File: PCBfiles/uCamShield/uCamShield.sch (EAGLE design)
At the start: 9 parts

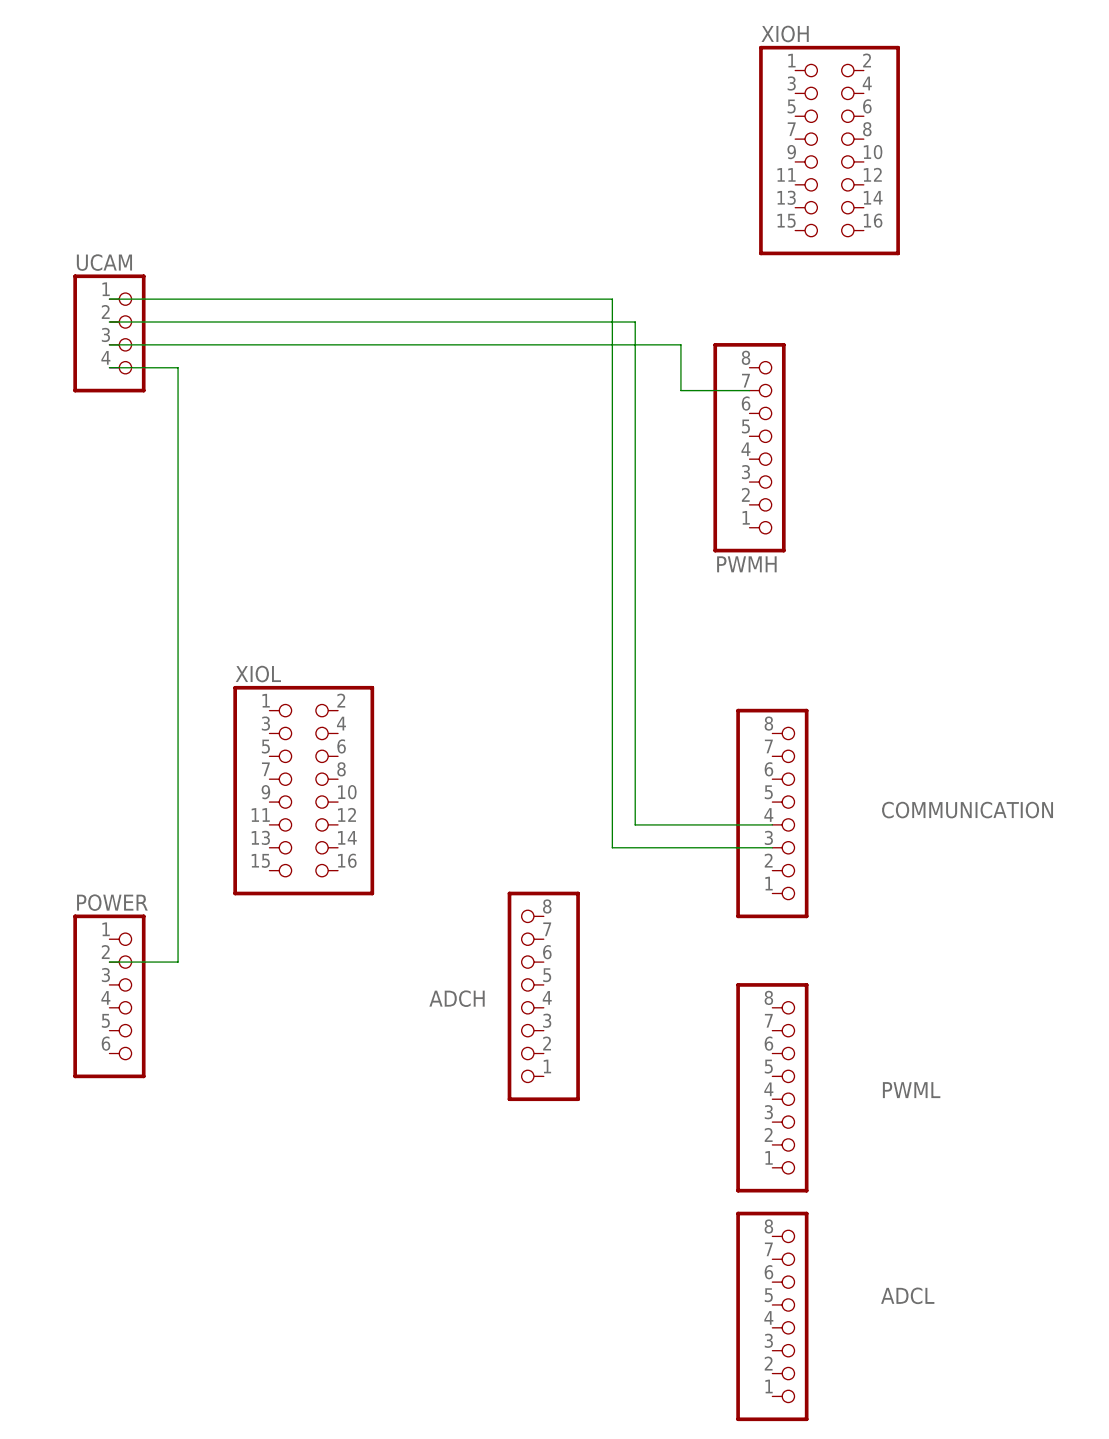
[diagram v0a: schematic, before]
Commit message: Fixed PCB file for uCam shield
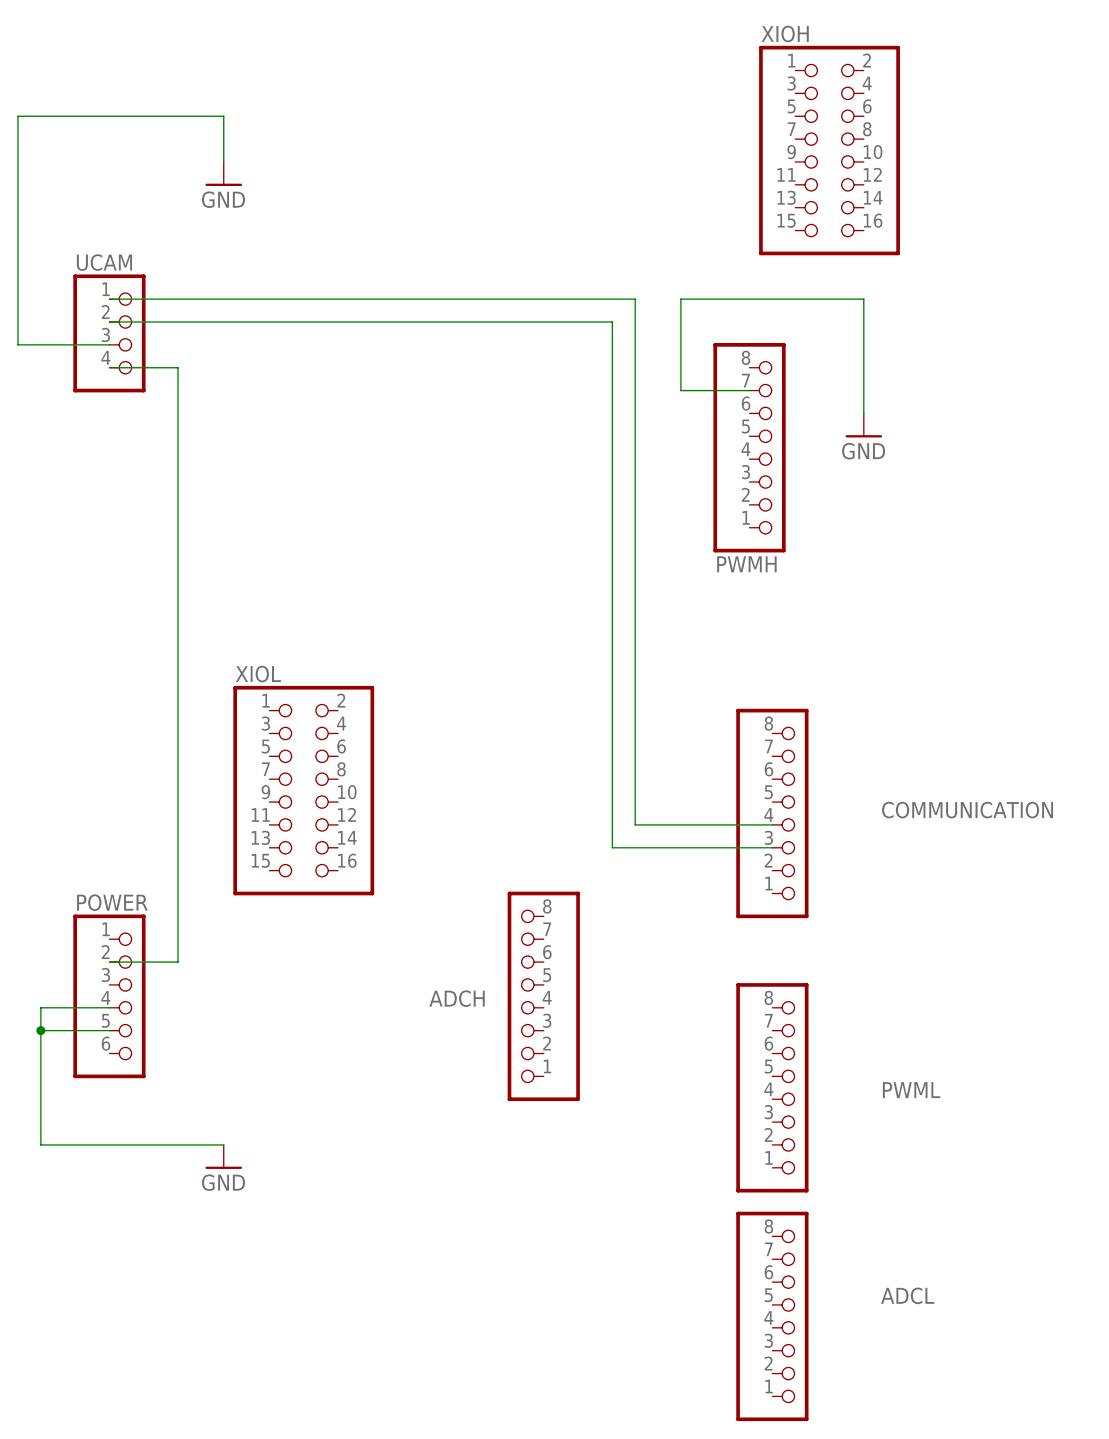
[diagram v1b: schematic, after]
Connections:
- removed net N$4: COMMUNICATION.3, UCAM.1
- new net GND: POWER.4, POWER.5, PWMH.7, UCAM.3
- net N$2: now also COMMUNICATION.4, UCAM.1; no longer PWMH.7, UCAM.3
- net N$3: now also COMMUNICATION.3; no longer COMMUNICATION.4
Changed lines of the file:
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@@
 <grid distance="0.1" unitdist="inch" unit="inch" style="lines" multiple="1" display="no" altdistance="0.01" altunitdist="inch" altunit="inch"/>
 <layers>
-<layer number="1" name="Top" color="4" fill="1" visible="yes" active="no"/>
-<layer number="2" name="Route2" color="1" fill="3" visible="yes" active="no"/>
-<layer number="3" name="Route3" color="4" fill="3" visible="yes" active="no"/>
-<layer number="14" name="Route14" color="1" fill="6" visible="yes" active="no"/>
-<layer number="15" name="Route15" color="4" fill="6" visible="yes" active="no"/>
-<layer number="16" name="Bottom" color="1" fill="1" visible="yes" active="no"/>
-<layer number="17" name="Pads" color="2" fill="1" visible="yes" active="no"/>
-<layer number="18" name="Vias" color="14" fill="1" visible="yes" active="no"/>
-<layer number="19" name="Unrouted" color="6" fill="1" visible="yes" active="no"/>
-<layer number="20" name="Dimension" color="15" fill="1" visible="yes" active="no"/>
-<layer number="21" name="tPlace" color="7" fill="1" visible="yes" active="no"/>
-<layer number="22" name="bPlace" color="7" fill="1" visible="yes" active="no"/>
-<layer number="23" name="tOrigins" color="15" fill="1" visible="yes" active="no"/>
-<layer number="24" name="bOrigins" color="15" fill="1" visible="yes" active="no"/>
-<layer number="25" name="tNames" color="7" fill="1" visible="yes" active="no"/>
-<layer number="26" name="bNames" color="7" fill="1" visible="yes" active="no"/>
-<layer number="27" name="tValues" color="7" fill="1" visible="yes" active="no"/>
-<layer number="28" name="bValues" color="7" fill="1" visible="yes" active="no"/>
+<layer number="1" name="Top" color="4" fill="1" visible="no" active="no"/>
+<layer number="2" name="Route2" color="1" fill="3" visible="no" active="no"/>
+<layer number="3" name="Route3" color="4" fill="3" visible="no" active="no"/>
+<layer number="14" name="Route14" color="1" fill="6" visible="no" active="no"/>
+<layer number="15" name="Route15" color="4" fill="6" visible="no" active="no"/>
+<layer number="16" name="Bottom" color="1" fill="1" visible="no" active="no"/>
+<layer number="17" name="Pads" color="2" fill="1" visible="no" active="no"/>
+<layer number="18" name="Vias" color="14" fill="1" visible="no" active="no"/>
+<layer number="19" name="Unrouted" color="6" fill="1" visible="no" active="no"/>
+<layer number="20" name="Dimension" color="15" fill="1" visible="no" active="no"/>
+<layer number="21" name="tPlace" color="7" fill="1" visible="no" active="no"/>
+<layer number="22" name="bPlace" color="7" fill="1" visible="no" active="no"/>
+<layer number="23" name="tOrigins" color="15" fill="1" visible="no" active="no"/>
+<layer number="24" name="bOrigins" color="15" fill="1" visible="no" active="no"/>
+<layer number="25" name="tNames" color="7" fill="1" visible="no" active="no"/>
+<layer number="26" name="bNames" color="7" fill="1" visible="no" active="no"/>
+<layer number="27" name="tValues" color="7" fill="1" visible="no" active="no"/>
+<layer number="28" name="bValues" color="7" fill="1" visible="no" active="no"/>
 <layer number="29" name="tStop" color="2" fill="3" visible="no" active="no"/>
 <layer number="30" name="bStop" color="5" fill="6" visible="no" active="no"/>
@@
 <layer number="35" name="tGlue" color="7" fill="4" visible="no" active="no"/>
 <layer number="36" name="bGlue" color="7" fill="5" visible="no" active="no"/>
-<layer number="37" name="tTest" color="7" fill="1" visible="yes" active="no"/>
-<layer number="38" name="bTest" color="7" fill="1" visible="yes" active="no"/>
+<layer number="37" name="tTest" color="7" fill="1" visible="no" active="no"/>
+<layer number="38" name="bTest" color="7" fill="1" visible="no" active="no"/>
 <layer number="39" name="tKeepout" color="4" fill="11" visible="no" active="no"/>
 <layer number="40" name="bKeepout" color="1" fill="11" visible="no" active="no"/>
@@
 <layer number="44" name="Drills" color="7" fill="1" visible="no" active="no"/>
 <layer number="45" name="Holes" color="7" fill="1" visible="no" active="no"/>
-<layer number="46" name="Milling" color="3" fill="1" visible="yes" active="no"/>
-<layer number="47" name="Measures" color="7" fill="1" visible="yes" active="no"/>
-<layer number="48" name="Document" color="7" fill="1" visible="yes" active="no"/>
-<layer number="49" name="Reference" color="13" fill="1" visible="yes" active="no"/>
-<layer number="50" name="dxf" color="12" fill="1" visible="yes" active="no"/>
-<layer number="51" name="tDocu" color="7" fill="1" visible="yes" active="no"/>
-<layer number="52" name="bDocu" color="7" fill="1" visible="yes" active="no"/>
-<layer number="53" name="tGND_GNDA" color="7" fill="1" visible="yes" active="no"/>
-<layer number="54" name="bGND_GNDA" color="7" fill="1" visible="yes" active="no"/>
-<layer number="56" name="wert" color="7" fill="1" visible="yes" active="no"/>
+<layer number="46" name="Milling" color="3" fill="1" visible="no" active="no"/>
+<layer number="47" name="Measures" color="7" fill="1" visible="no" active="no"/>
+<layer number="48" name="Document" color="7" fill="1" visible="no" active="no"/>
+<layer number="49" name="Reference" color="13" fill="1" visible="no" active="no"/>
+<layer number="50" name="dxf" color="12" fill="1" visible="no" active="no"/>
+<layer number="51" name="tDocu" color="7" fill="1" visible="no" active="no"/>
+<layer number="52" name="bDocu" color="7" fill="1" visible="no" active="no"/>
+<layer number="53" name="tGND_GNDA" color="7" fill="1" visible="no" active="no"/>
+<layer number="54" name="bGND_GNDA" color="7" fill="1" visible="no" active="no"/>
+<layer number="56" name="wert" color="7" fill="1" visible="no" active="no"/>
 <layer number="91" name="Nets" color="2" fill="1" visible="yes" active="yes"/>
 <layer number="92" name="Busses" color="1" fill="1" visible="yes" active="yes"/>
@@
 <part name="XIOL" library="pinhead" deviceset="PINHD-2X8" device=""/>
 <part name="UCAM" library="pinhead" deviceset="PINHD-1X4" device=""/>
+<part name="GND1" library="supply1" deviceset="GND" device=""/>
+<part name="GND2" library="supply1" deviceset="GND" device=""/>
+<part name="GND3" library="supply1" deviceset="GND" device=""/>
 </parts>
 <sheets>
@@
 <instance part="XIOL" gate="A" x="43.18" y="66.04"/>
 <instance part="UCAM" gate="A" x="25.4" y="114.3"/>
+<instance part="GND1" gate="1" x="35.56" y="132.08"/>
+<instance part="GND2" gate="1" x="106.68" y="104.14"/>
+<instance part="GND3" gate="1" x="35.56" y="22.86"/>
 </instances>
 <busses>
@@
 </segment>
 </net>
+<net name="GND" class="0">
+<segment>
+<pinref part="PWMH" gate="A" pin="7"/>
+<wire x1="86.36" y1="109.22" x2="93.98" y2="109.22" width="0.1524" layer="91"/>
+<wire x1="86.36" y1="109.22" x2="86.36" y2="119.38" width="0.1524" layer="91"/>
+<pinref part="GND2" gate="1" pin="GND"/>
+<wire x1="86.36" y1="119.38" x2="106.68" y2="119.38" width="0.1524" layer="91"/>
+<wire x1="106.68" y1="119.38" x2="106.68" y2="106.68" width="0.1524" layer="91"/>
+</segment>
+<segment>
+<pinref part="UCAM" gate="A" pin="3"/>
+<wire x1="22.86" y1="114.3" x2="12.7" y2="114.3" width="0.1524" layer="91"/>
+<wire x1="12.7" y1="114.3" x2="12.7" y2="139.7" width="0.1524" layer="91"/>
+<pinref part="GND1" gate="1" pin="GND"/>
+<wire x1="12.7" y1="139.7" x2="35.56" y2="139.7" width="0.1524" layer="91"/>
+<wire x1="35.56" y1="139.7" x2="35.56" y2="134.62" width="0.1524" layer="91"/>
+</segment>
+<segment>
+<pinref part="POWER" gate="A" pin="4"/>
+<wire x1="22.86" y1="40.64" x2="15.24" y2="40.64" width="0.1524" layer="91"/>
+<wire x1="15.24" y1="40.64" x2="15.24" y2="38.1" width="0.1524" layer="91"/>
+<pinref part="GND3" gate="1" pin="GND"/>
+<wire x1="15.24" y1="38.1" x2="15.24" y2="25.4" width="0.1524" layer="91"/>
+<wire x1="15.24" y1="25.4" x2="35.56" y2="25.4" width="0.1524" layer="91"/>
+<pinref part="POWER" gate="A" pin="5"/>
+<wire x1="22.86" y1="38.1" x2="15.24" y2="38.1" width="0.1524" layer="91"/>
+<junction x="15.24" y="38.1"/>
+</segment>
+</net>
 <net name="N$2" class="0">
 <segment>
-<pinref part="UCAM" gate="A" pin="3"/>
-<wire x1="22.86" y1="114.3" x2="86.36" y2="114.3" width="0.1524" layer="91"/>
-<wire x1="86.36" y1="114.3" x2="86.36" y2="109.22" width="0.1524" layer="91"/>
-<pinref part="PWMH" gate="A" pin="7"/>
-<wire x1="86.36" y1="109.22" x2="93.98" y2="109.22" width="0.1524" layer="91"/>
+<pinref part="UCAM" gate="A" pin="1"/>
+<wire x1="22.86" y1="119.38" x2="81.28" y2="119.38" width="0.1524" layer="91"/>
+<wire x1="81.28" y1="119.38" x2="81.28" y2="60.96" width="0.1524" layer="91"/>
+<pinref part="COMMUNICATION" gate="A" pin="4"/>
+<wire x1="81.28" y1="60.96" x2="96.52" y2="60.96" width="0.1524" layer="91"/>
 </segment>
 </net>
@@
 <segment>
 <pinref part="UCAM" gate="A" pin="2"/>
-<wire x1="22.86" y1="116.84" x2="81.28" y2="116.84" width="0.1524" layer="91"/>
-<wire x1="81.28" y1="116.84" x2="81.28" y2="60.96" width="0.1524" layer="91"/>
-<pinref part="COMMUNICATION" gate="A" pin="4"/>
-<wire x1="81.28" y1="60.96" x2="96.52" y2="60.96" width="0.1524" layer="91"/>
-</segment>
-</net>
-<net name="N$4" class="0">
-<segment>
-<pinref part="UCAM" gate="A" pin="1"/>
-<wire x1="22.86" y1="119.38" x2="78.74" y2="119.38" width="0.1524" layer="91"/>
-<wire x1="78.74" y1="119.38" x2="78.74" y2="58.42" width="0.1524" layer="91"/>
+<wire x1="22.86" y1="116.84" x2="78.74" y2="116.84" width="0.1524" layer="91"/>
+<wire x1="78.74" y1="116.84" x2="78.74" y2="58.42" width="0.1524" layer="91"/>
 <pinref part="COMMUNICATION" gate="A" pin="3"/>
 <wire x1="78.74" y1="58.42" x2="96.52" y2="58.42" width="0.1524" layer="91"/>
